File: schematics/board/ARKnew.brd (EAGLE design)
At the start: 89 x 89 mm, 213 parts, among them IC2 STM32F103C8T, Q5 8MHz

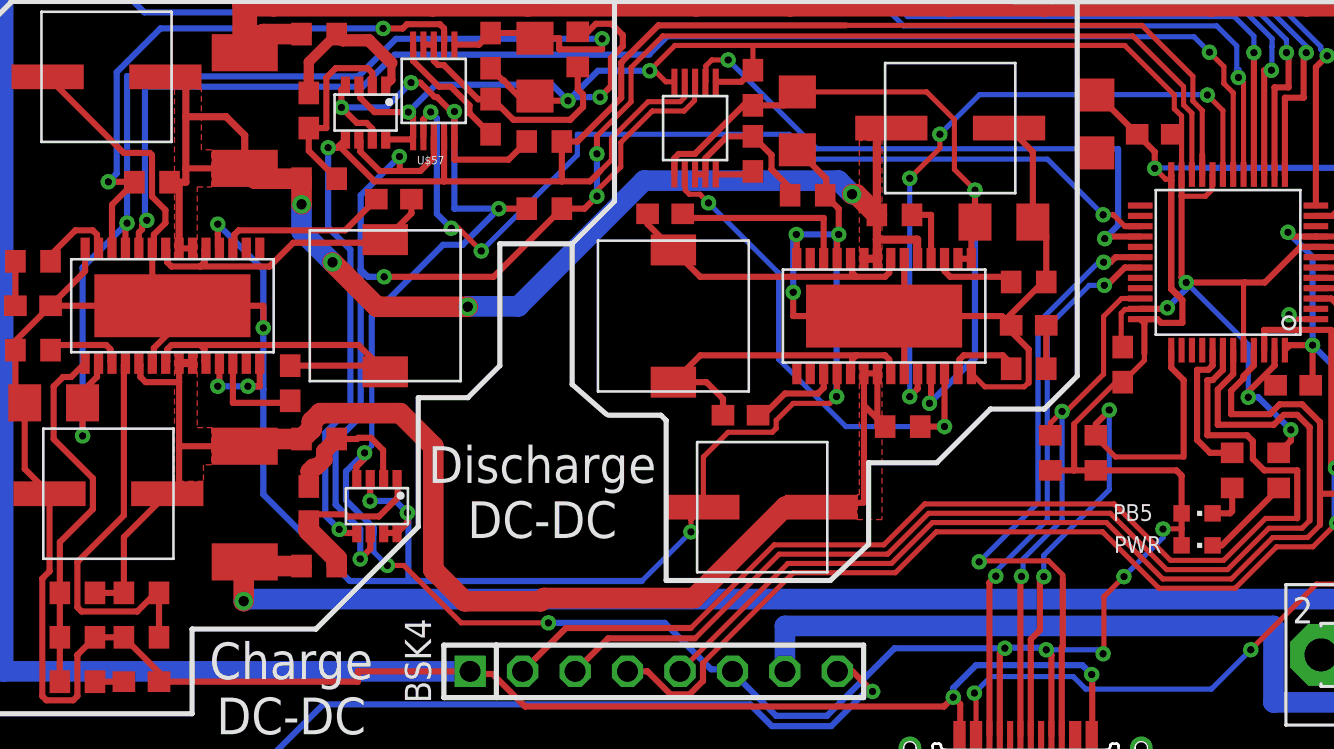
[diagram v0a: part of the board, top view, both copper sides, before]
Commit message: Обновлена плата АРК
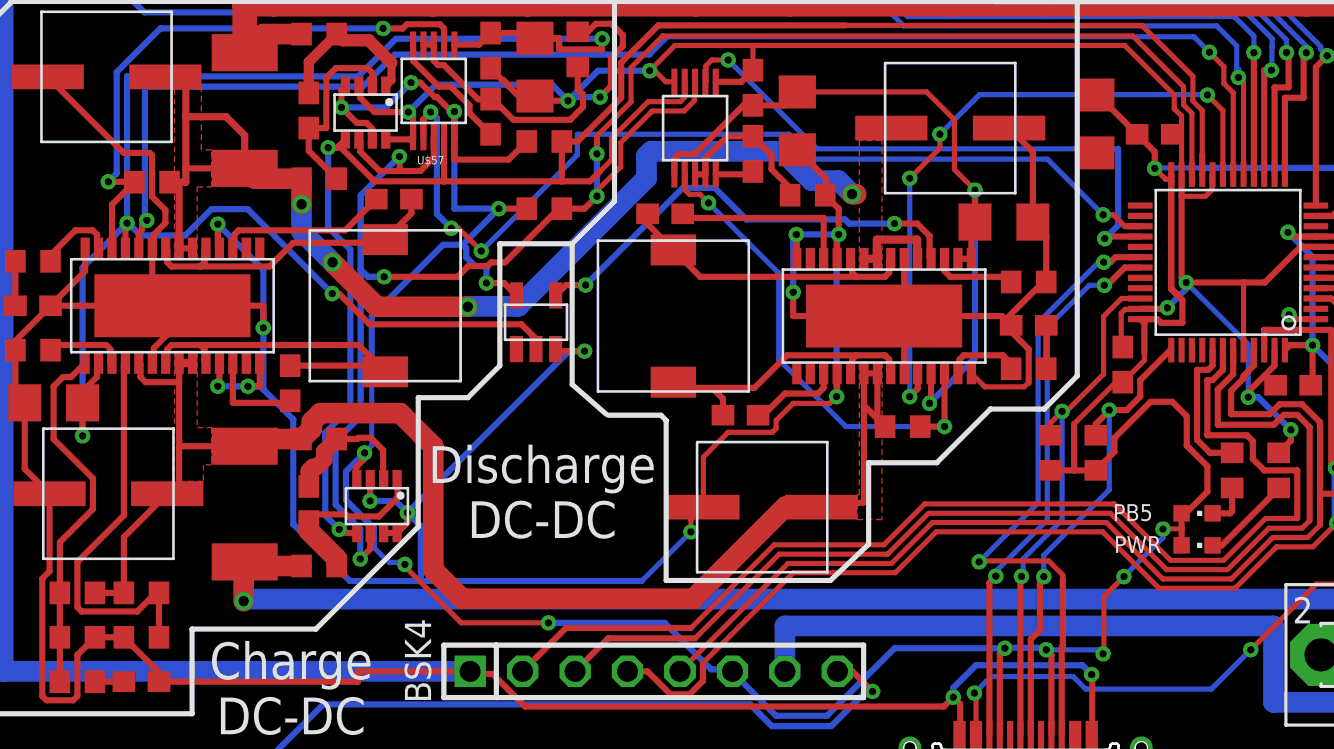
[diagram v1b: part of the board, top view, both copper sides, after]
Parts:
- removed R63: 1M, resistor:R0603
- added U$2: INVERTER, CanCubeSat:INVERTER
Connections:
- removed net N$45: C32.1, C39.1, C43.1, U$59.11, U$59.16, U$60.1
- removed net N$53: R63.1, U$16.18
- new net A: C32.1, C39.1, C43.1, U$2.P$2, U$59.11, U$59.16, U$60.1
- new net Y: U$16.18, U$2.P$4
- net GND: now also U$2.P$3
- net INA_BMS+: no longer R63.2
- net VDD: now also U$2.P$5
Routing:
- net A: track 0.00 -> 79.4 mm, vias 0 -> 4
- net N$45: track 55.7 -> 0.00 mm, vias 3 -> 0
- net Y: track 0.00 -> 22.4 mm, vias 0 -> 2
- net GND: track 556.0 -> 569.5 mm, vias 27 -> 28
- net VDD: track 309.5 -> 319.8 mm, vias 19 -> 20
- net SWC: track 29.0 -> 23.5 mm
- net INA_BMS+: track 67.6 -> 62.5 mm
- net N$53: track 3.05 -> 0.00 mm

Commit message: АРК 2.0
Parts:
- added U$22, U$27, U$28, U$29, U$30, U$9: FS8205A-, CanCubeSat:FS8205A-
- moved R93 0.10 mm to (48.5, 49.8)
- moved R95 0.10 mm to (23.5, 49.8)
- moved R94 0.10 mm to (21.2, 49.8)
- moved R91 0.10 mm to (73.5, 49.8)
- moved R90 0.05 mm to (71.2, 49.8)
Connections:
- new net N$31: R91.2, U$9.5
- new net N$45: R90.2, U$9.4
- new net N$49: U$15.23, U$22.67
- new net N$50: U$24.23, U$9.67
- new net N$53: R88.2, U$22.4
- new net N$61: R89.2, U$22.5
- new net N$62: U$25.23, U$27.67
- new net N$63: R93.2, U$27.5
- new net N$64: R92.2, U$27.4
- new net N$73: U$28.67, U$8.23
- new net N$74: R97.2, U$28.5
- new net N$77: R96.2, U$28.4
- new net N$79: U$26.23, U$29.67
- new net N$80: R95.2, U$29.5
- new net N$89: R94.2, U$29.4
- new net N$90: U$1.23, U$30.67
- new net N$93: R99.2, U$30.5
- new net N$95: R98.2, U$30.4
- net GND: now also U$22.23, U$27.23, U$28.23, U$29.23, U$30.23, U$9.23; no longer U$1.23, U$15.23, U$24.23, U$25.23, U$26.23, U$8.23
- net OC1: no longer R95.2
- net OC2: no longer R99.2
- net OC3: no longer R93.2
- net OC4: no longer R97.2
- net OC5: no longer R91.2
- net OC6: no longer R89.2
- net OD1: no longer R94.2
- net OD2: no longer R98.2
- net OD3: no longer R92.2
- net OD4: no longer R96.2
- net OD5: no longer R90.2
- net OD6: no longer R88.2
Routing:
- net N$95: track 0.00 -> 14.6 mm, vias 0 -> 3
- net N$77: track 0.00 -> 14.6 mm, vias 0 -> 3
- net N$53: track 0.00 -> 14.5 mm, vias 0 -> 3
- net N$89: track 0.00 -> 14.3 mm, vias 0 -> 3
- net N$64: track 0.00 -> 14.3 mm, vias 0 -> 3
- net N$45: track 0.00 -> 14.2 mm, vias 0 -> 3
- net OD4: track 9.13 -> 1.63 mm
- net OD6: track 8.93 -> 1.63 mm
- net OD2: track 8.73 -> 1.63 mm
- net OD1: track 8.63 -> 1.63 mm
- net OD3: track 8.63 -> 1.63 mm
- net OD5: track 8.63 -> 1.63 mm
- net N$93: track 0.00 -> 6.19 mm, vias 0 -> 1
- net N$61: track 0.00 -> 6.16 mm, vias 0 -> 1
- net N$74: track 0.00 -> 6.12 mm, vias 0 -> 1
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
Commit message: Исправлены диоды в АРКе
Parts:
- moved LED3 0.28 mm to (64.3, 49.6), turned to 0 degrees
- moved LED6 0.28 mm to (39.3, 49.6), turned to 0 degrees
- moved LED7 0.28 mm to (26.6, 49.6), turned to 0 degrees
- moved LED4 0.25 mm to (76.6, 49.5), turned to 0 degrees
- moved LED5 0.25 mm to (51.6, 49.6), turned to 0 degrees
- moved LED8 0.21 mm to (14.3, 49.6), turned to 0 degrees
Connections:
- net BMS+: now also LED3.A, LED4.A, LED5.A, LED6.A, LED7.A, LED8.A; no longer LED3.C, LED4.C, LED5.C, LED6.C, LED7.C, LED8.C
- net N$54: now also LED3.C; no longer LED3.A
- net N$56: now also LED4.C; no longer LED4.A
- net N$57: now also LED5.C; no longer LED5.A
- net N$58: now also LED6.C; no longer LED6.A
- net N$59: now also LED7.C; no longer LED7.A
- net N$60: now also LED8.C; no longer LED8.A

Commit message: Изменен АРК
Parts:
- removed C32: 0,1µ, rcl:C0603
- removed C42: 1µ, rcl:C0603
- removed C43: 10µ, rcl:C1206
- removed LED4, LED5, LED6, LED7: (no value), led:CHIPLED_0603
- removed R80, R83, R84, R85, R86: 2k, resistor:R0603
- removed U$60: AD5272, CanCubeSat:AD5272
- added LED1, LED2: (no value), led:CHIPLED_0603
- added R31, R32, R57: 2k, resistor:R0603
- R70: value 14k3 -> 24k3
- R72: value 91k -> 232k
- moved LED3 25.2 mm to (53.2, 27.0), turned to 180 degrees
- moved LED8 13.4 mm to (7.00, 38.4)
- moved R100 12.8 mm to (7.00, 41.7), turned to 270 degrees
- moved C35 2.98 mm to (14.0, 44.4)
- moved R75 2.90 mm to (20.6, 42.3)
- moved C34 2.90 mm to (27.8, 38.0)
- moved C41 2.90 mm to (23.7, 42.3)
- moved R76 2.90 mm to (24.2, 46.0)
- moved R77 2.90 mm to (24.2, 39.0)
- moved U$57 2.90 mm to (26.4, 42.2)
- moved R72 2.20 mm to (15.4, 38.9)
- moved R27 1.45 mm to (60.4, 25.8)
- moved R64 1.20 mm to (57.9, 25.7)
- moved U$13 0.05 mm to (54.5, 60.9), turned to 180 degrees
- moved U$14 0.05 mm to (50.9, 60.9), turned to 180 degrees
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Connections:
- removed net DPC_RST: IC2.27, U$60.7
- removed net N$101: R52.1, U$48.2
- removed net N$103: R53.1, U$49.2
- removed net N$154: C42.1, U$60.5
- removed net N$87: R45.1, U$42.2
- net A: now also LED8.A; no longer C32.1, C43.1, U$60.1
- net B-1: now also U$7.2; no longer R86.1, U$7.3
- net B-2: now also U$49.2; no longer R100.1, U$49.3
- net B-3: now also U$14.2; no longer R84.1, U$14.3
- net B-4: now also U$42.2; no longer R85.1, U$42.3
- net B-5: now also U$21.2; no longer R83.1, U$21.3
- net B-6: now also U$35.2; no longer R80.1, U$35.3
- net BMS+: no longer LED3.A, LED4.A, LED5.A, LED6.A, LED7.A, LED8.A
- net GND: now also R100.1, R31.1, R32.1, R57.1; no longer C32.2, C43.2, U$60.6
- net N$10: now also U$7.3; no longer U$7.2
- net N$110: now also U$48.2; no longer U$48.3
- net N$21: now also U$13.3; no longer U$13.2
- net N$23: now also U$14.3; no longer U$14.2
- net N$25: now also R70.1; no longer U$60.2
- net N$26: now also LED1.C, R31.2; no longer C42.2, R70.1, U$60.3, U$60.4
- net N$30: now also U$13.2; no longer U$13.3
- net N$37: now also U$20.3; no longer U$20.2
- net N$39: now also U$21.3; no longer U$21.2
- net N$46: now also U$20.2; no longer U$20.3
- net N$47: now also LED1.A
- net N$54: now also LED2.C, R32.2; no longer LED3.C, R80.2
- net N$56: now also LED3.C, R57.2; no longer LED4.C, R83.2
- net N$57: now also R36.1, U$34.3; no longer LED5.C, R84.2
- net N$58: now also R37.1, U$35.3; no longer LED6.C, R85.2
- net N$59: now also R44.1, U$41.3; no longer LED7.C, R86.2
- net N$69: now also R45.1, U$42.3; no longer R36.1, U$34.2
- net N$7: now also U$6.3; no longer U$6.2
- net N$71: now also R52.1, U$48.3; no longer R37.1, U$35.2
- net N$78: now also U$34.2; no longer U$34.3
- net N$8: now also U$6.2; no longer U$6.3
- net N$85: now also R53.1, U$49.3; no longer R44.1, U$41.2
- net N$94: now also U$41.2; no longer U$41.3
- net PGOOD1: now also LED2.A
- net PGOOD2: now also LED3.A
- net SCL: no longer U$60.9
- net SDA: no longer U$60.8
- net VDD: no longer U$60.10
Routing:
- net DPC_RST: track 46.0 -> 0.00 mm, vias 4 -> 0
- net A: track 79.4 -> 46.0 mm
- net GND: track 568.7 -> 580.9 mm
- net BMS+: track 246.6 -> 235.1 mm
- net N$26: track 12.0 -> 2.44 mm
- net INA_BMS+: track 66.7 -> 74.2 mm
- net PGOOD2: track 32.5 -> 39.7 mm
- net N$154: track 6.23 -> 0.00 mm
- net B-4: track 35.9 -> 30.5 mm
- net B-3: track 35.8 -> 30.4 mm
- net B-6: track 36.0 -> 30.6 mm
- net B-5: track 35.8 -> 30.5 mm
- net B-1: track 35.7 -> 30.4 mm
- net VDD: track 319.8 -> 314.5 mm, vias 20 -> 21
- net B-2: track 35.8 -> 30.5 mm
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
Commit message: Подготовлены к производству платы ARK v1.1 и SP v 1.2
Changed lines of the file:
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@@
 <drawing>
 <settings>
-<setting alwaysvectorfont="no"/>
+<setting alwaysvectorfont="yes"/>
 <setting verticaltext="up"/>
 </settings>
@@
 <layer number="14" name="Route14" color="22" fill="1" visible="no" active="no"/>
 <layer number="15" name="Route15" color="23" fill="1" visible="no" active="no"/>
-<layer number="16" name="Bottom" color="1" fill="1" visible="yes" active="yes"/>
+<layer number="16" name="Bottom" color="1" fill="1" visible="no" active="yes"/>
 <layer number="17" name="Pads" color="2" fill="1" visible="yes" active="yes"/>
 <layer number="18" name="Vias" color="2" fill="1" visible="yes" active="yes"/>
@@
 <layer number="20" name="Dimension" color="24" fill="1" visible="yes" active="yes"/>
 <layer number="21" name="tPlace" color="7" fill="1" visible="yes" active="yes"/>
-<layer number="22" name="bPlace" color="7" fill="1" visible="yes" active="yes"/>
+<layer number="22" name="bPlace" color="7" fill="1" visible="no" active="yes"/>
 <layer number="23" name="tOrigins" color="15" fill="1" visible="yes" active="yes"/>
-<layer number="24" name="bOrigins" color="15" fill="1" visible="yes" active="yes"/>
+<layer number="24" name="bOrigins" color="15" fill="1" visible="no" active="yes"/>
 <layer number="25" name="tNames" color="7" fill="1" visible="yes" active="yes"/>
-<layer number="26" name="bNames" color="7" fill="1" visible="yes" active="yes"/>
-<layer number="27" name="tValues" color="7" fill="1" visible="yes" active="yes"/>
+<layer number="26" name="bNames" color="7" fill="1" visible="no" active="yes"/>
+<layer number="27" name="tValues" color="7" fill="1" visible="no" active="yes"/>
 <layer number="28" name="bValues" color="7" fill="1" visible="no" active="yes"/>
-<layer number="29" name="tStop" color="7" fill="3" visible="yes" active="yes"/>
+<layer number="29" name="tStop" color="7" fill="3" visible="no" active="yes"/>
 <layer number="30" name="bStop" color="7" fill="6" visible="no" active="yes"/>
 <layer number="31" name="tCream" color="7" fill="4" visible="no" active="yes"/>
@@
 <layer number="38" name="bTest" color="7" fill="1" visible="no" active="yes"/>
 <layer number="39" name="tKeepout" color="4" fill="11" visible="yes" active="yes"/>
-<layer number="40" name="bKeepout" color="1" fill="11" visible="yes" active="yes"/>
+<layer number="40" name="bKeepout" color="1" fill="11" visible="no" active="yes"/>
 <layer number="41" name="tRestrict" color="4" fill="10" visible="yes" active="yes"/>
-<layer number="42" name="bRestrict" color="1" fill="10" visible="yes" active="yes"/>
+<layer number="42" name="bRestrict" color="1" fill="10" visible="no" active="yes"/>
 <layer number="43" name="vRestrict" color="2" fill="10" visible="no" active="yes"/>
 <layer number="44" name="Drills" color="7" fill="1" visible="no" active="yes"/>
-<layer number="45" name="Holes" color="7" fill="1" visible="yes" active="yes"/>
+<layer number="45" name="Holes" color="7" fill="1" visible="no" active="yes"/>
 <layer number="46" name="Milling" color="3" fill="1" visible="no" active="yes"/>
 <layer number="47" name="Measures" color="7" fill="1" visible="no" active="yes"/>
@@
 <layer number="50" name="dxf" color="7" fill="1" visible="no" active="yes"/>
 <layer number="51" name="tDocu" color="7" fill="1" visible="yes" active="yes"/>
-<layer number="52" name="bDocu" color="7" fill="1" visible="yes" active="yes"/>
+<layer number="52" name="bDocu" color="7" fill="1" visible="no" active="yes"/>
 <layer number="53" name="tGND_GNDA" color="7" fill="9" visible="no" active="no"/>
 <layer number="54" name="bGND_GNDA" color="1" fill="9" visible="no" active="no"/>
@@
 <wire x1="30.05" y1="30" x2="30.05" y2="35.9" width="0.25" layer="21"/>
 <text x="1.5" y="69.85" size="1.4224" layer="21">BMS</text>
-<text x="19.95" y="16.6" size="1.778" layer="21" align="top-center">Charge
-DC-DC</text>
+<text x="13.65" y="12.8" size="1.778" layer="21" align="top-center">Charge DC-DC</text>
 <wire x1="19.1" y1="71.05" x2="19.1" y2="47.95" width="0.25" layer="21"/>
 <wire x1="44.25" y1="71.05" x2="44.25" y2="47.9" width="0.25" layer="21"/>
 <wire x1="69.1" y1="71.05" x2="69.1" y2="47.9" width="0.25" layer="21"/>
-<text x="32.1" y="26.1" size="1.778" layer="21" align="top-center">Discharge
-DC-DC</text>
+<text x="47.8" y="19.25" size="1.778" layer="21" align="top-center">Discharge DC-DC</text>
 <wire x1="58" y1="47.6" x2="58" y2="29.25" width="0.25" layer="21"/>
 <wire x1="55.3" y1="22.35" x2="47.9" y2="22.35" width="0.25" layer="21"/>
@@
 <text x="77.95" y="25.7" size="1.27" layer="21" align="top-center">SDATM</text>
 <text x="78" y="23.15" size="1.27" layer="21" align="top-center">SCLTM</text>
-<text x="35.1" y="82" size="0.9" layer="21" rot="R90" align="top-center">B-4</text>
-<text x="37.65" y="82" size="0.9" layer="21" rot="R90" align="top-center">BC4</text>
-<text x="40.15" y="82" size="0.9" layer="21" rot="R90" align="top-center">VDD</text>
-<text x="42.75" y="82" size="0.9" layer="21" rot="R90" align="top-center">GND</text>
-<text x="45.3" y="82" size="0.9" layer="21" rot="R90" align="top-center">1W</text>
-<text x="48" y="82" size="0.9" layer="21" rot="R90" align="top-center">B-3</text>
-<text x="50.35" y="82" size="0.9" layer="21" rot="R90" align="top-center">BC3</text>
-<text x="53" y="82" size="0.9" layer="21" rot="R90" align="top-center">B+</text>
-<text x="28.25" y="7.05" size="0.9" layer="21" rot="R90" align="top-center">GND</text>
-<text x="30.8" y="7.05" size="0.9" layer="21" rot="R90" align="top-center">TIME</text>
-<text x="33.3" y="7.05" size="0.9" layer="21" rot="R90" align="top-center">INT</text>
-<text x="35.9" y="7.05" size="0.9" layer="21" rot="R90" align="top-center">SDA</text>
-<text x="38.45" y="7.05" size="0.9" layer="21" rot="R90" align="top-center">SCL</text>
-<text x="41.15" y="7.05" size="0.9" layer="21" rot="R90" align="top-center">VDD</text>
-<text x="43.5" y="7.05" size="0.9" layer="21" rot="R90" align="top-center">BUS+</text>
-<text x="46.15" y="7.05" size="0.9" layer="21" rot="R90" align="top-center">5V</text>
+<text x="35.1" y="83.2" size="0.9" layer="21" rot="R90" align="center-right">B-4</text>
+<text x="37.65" y="83.2" size="0.9" layer="21" rot="R90" align="center-right">BC4</text>
+<text x="40.15" y="83.2" size="0.9" layer="21" rot="R90" align="center-right">VDD</text>
+<text x="42.75" y="83.2" size="0.9" layer="21" rot="R90" align="center-right">GND</text>
+<text x="45.3" y="83.2" size="0.9" layer="21" rot="R90" align="center-right">1W</text>
+<text x="48" y="83.2" size="0.9" layer="21" rot="R90" align="center-right">B-3</text>
+<text x="50.35" y="83.2" size="0.9" layer="21" rot="R90" align="center-right">BC3</text>
+<text x="53" y="83.2" size="0.9" layer="21" rot="R90" align="center-right">B+</text>
+<text x="28.25" y="5.8" size="0.9" layer="21" rot="R90" align="center-left">GND</text>
+<text x="30.8" y="5.8" size="0.9" layer="21" rot="R90" align="center-left">TIME</text>
+<text x="33.3" y="5.8" size="0.9" layer="21" rot="R90" align="center-left">INT</text>
+<text x="35.9" y="5.8" size="0.9" layer="21" rot="R90" align="center-left">SDA</text>
+<text x="38.45" y="5.8" size="0.9" layer="21" rot="R90" align="center-left">SCL</text>
+<text x="41.15" y="5.8" size="0.9" layer="21" rot="R90" align="center-left">VDD</text>
+<text x="43.5" y="5.8" size="0.9" layer="21" rot="R90" align="center-left">BUS+</text>
+<text x="46.15" y="5.8" size="0.9" layer="21" rot="R90" align="center-left">5V</text>
 <wire x1="55.35" y1="22.4" x2="56.45" y2="23.5" width="0.25" layer="21"/>
 <wire x1="56.45" y1="23.5" x2="56.45" y2="27.7" width="0.25" layer="21"/>
@@
 </drawing>
 <compatibility>
-<note version="6.3" minversion="6.2.2" severity="warning">
-Since Version 6.2.2 text objects can contain more than one line,
-which will not be processed correctly with this version.
-</note>
 <note version="8.2" severity="warning">
 Since Version 8.2, EAGLE supports online libraries. The ids
